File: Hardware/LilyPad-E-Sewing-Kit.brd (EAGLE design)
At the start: 45.7 x 50.8 mm, 57 parts

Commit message: Updated board files
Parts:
- added U$8: OSHW-LOGOS, SparkFun-Aesthetics:OSHW-LOGO-S
- added U$9: (no value), SparkFun-Aesthetics:SFE-LOGO-FLAME
- turned U$5 to 90 degrees
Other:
- board text removed: "12/5/2011"

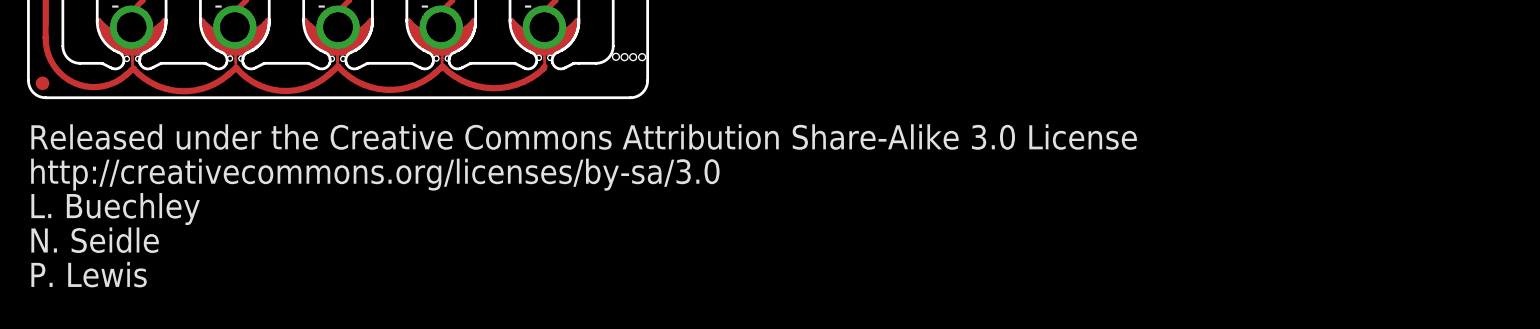
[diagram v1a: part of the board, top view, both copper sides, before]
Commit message: Fixed labeling on board.
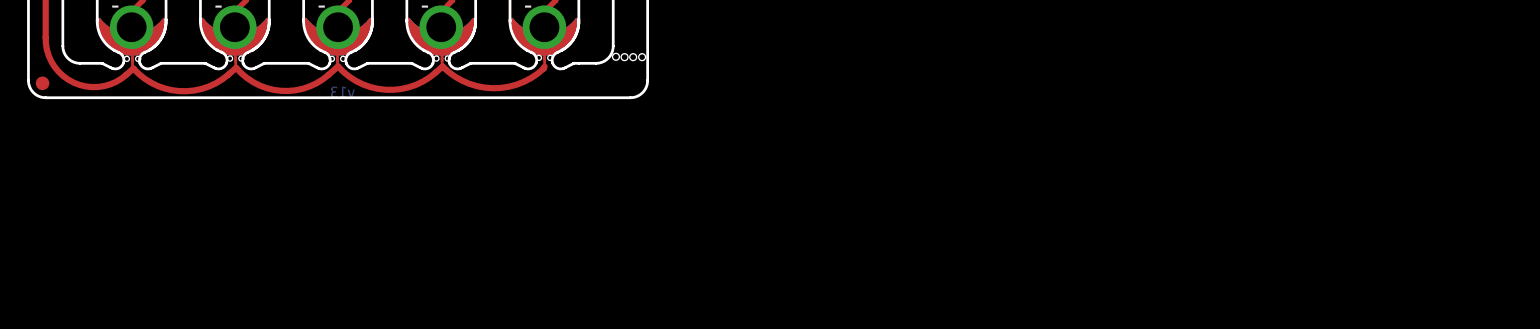
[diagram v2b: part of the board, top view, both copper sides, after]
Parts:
- added JP2: LOGO-SFESK, SparkFun-Aesthetics:SFE-LOGO-FLAME
- U$9: device SparkFun-Aesthetics:SFE-LOGO-FLAME -> SparkFun-Aesthetics:CREATIVE_COMMONS
- moved U$9 35.9 mm to (3.81, -11.4), flipped to the top
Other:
- board text added: "L. Buechley, N. Seidle, P. Lewis, T. Klopfenstein"
- board text added: "v13"
- board text removed: "L. Buechley"
- board text removed: "N. Seidle"
- board text removed: "P. Lewis"
- board text removed: "Released under the Creative Commons Attribution Share-Alike 3.0 License"
- board text removed: "http://creativecommons.org/licenses/by-sa/3.0"
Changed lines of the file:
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@@
 <wire x1="20.701" y1="16.51" x2="17.399" y2="16.51" width="0.2032" layer="20"/>
 <wire x1="13.081" y1="16.51" x2="9.779" y2="16.51" width="0.2032" layer="20"/>
-<text x="0" y="-8.89" size="1.778" layer="21">L. Buechley</text>
-<text x="0" y="-11.43" size="1.778" layer="21">N. Seidle</text>
-<text x="0" y="-3.81" size="1.778" layer="21">Released under the Creative Commons Attribution Share-Alike 3.0 License</text>
-<text x="0" y="-6.35" size="1.778" layer="21">http://creativecommons.org/licenses/by-sa/3.0</text>
 <text x="29.464" y="39.116" size="1.016" layer="21" font="vector" ratio="15" rot="R90">On</text>
 <text x="29.464" y="30.226" size="1.016" layer="21" font="vector" ratio="15" rot="R90">Off</text>
@@
 <text x="9.779" y="12.827" size="1.4224" layer="21" ratio="15" rot="R180">+</text>
 <text x="6.731" y="7.62" size="1.4224" layer="21" ratio="15" rot="R180">-</text>
-<text x="0" y="-13.97" size="1.778" layer="21">P. Lewis</text>
 <text x="18.542" y="45.593" size="2.54" layer="21" font="vector" ratio="15" rot="R90">+</text>
 <text x="4.191" y="47.752" size="2.54" layer="21" font="vector" ratio="15" rot="R270">-</text>
 <text x="16.129" y="24.892" size="2.54" layer="21" font="vector" ratio="15" rot="R270">+</text>
 <text x="6.731" y="22.733" size="2.54" layer="21" font="vector" ratio="15" rot="R90">-</text>
-<text x="43.18" y="20.32" size="1.778" layer="22" font="vector" ratio="15" rot="MR0">E-sewing Kit</text>
+<text x="44.45" y="20.32" size="1.778" layer="22" font="vector" ratio="15" rot="MR0">E-sewing Kit</text>
 <rectangle x1="32.258" y1="34.29" x2="33.401" y2="36.83" layer="21" rot="R180"/>
 <hole x="1.778" y="24.257" drill="0.508"/>
@@
 <hole x="44.704" y="16.0274" drill="0.508"/>
 <hole x="45.3644" y="16.0274" drill="0.508"/>
+<text x="34.29" y="-11.43" size="1.778" layer="27" font="vector" ratio="15">L. Buechley, N. Seidle, P. Lewis, T. Klopfenstein</text>
+<text x="24.13" y="0" size="0.8128" layer="16" font="vector" ratio="25" rot="MR0">v13</text>
 </plain>
 <attributes>
@@
 <element name="JP1" library="SparkFun" package="FIDUCIAL-1X2" value="FIDUCIAL1X2" x="44.577" y="49.657"/>
 <element name="U$8" library="SparkFun-Aesthetics" package="OSHW-LOGO-S" value="OSHW-LOGOS" x="2.54" y="19.05" rot="MR0"/>
-<element name="U$9" library="SparkFun-Aesthetics" package="SFE-LOGO-FLAME" value="" x="22.86" y="19.05" rot="MR0"/>
+<element name="U$9" library="SparkFun-Aesthetics" package="CREATIVE_COMMONS" value="" x="3.81" y="-11.43"/>
+<element name="JP2" library="SparkFun-Aesthetics" package="SFE-LOGO-FLAME" value="LOGO-SFESK" x="25.4" y="20.32" rot="MR0"/>
 </elements>
 <signals>
